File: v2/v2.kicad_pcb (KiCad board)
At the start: 4 copper layers, 45.5 x 52 mm, 73 parts, among them J1 Conn_01x02_Pin, J2 Conn_01x09_Pin, J3 Conn_01x20_Socket, J4 Conn_01x20_Socket, U1 ADS1299IPAGR, U11 TPS73225DBVR, U3 TPD4E1B06DCKR, U4 TPD4E1B06DCKR, U5 LM2664M6, U6 TPS61023DRLR, U7 TPS73233DBVT, U8 TPS72325DBVT, U9 TPD4E1B06DCKR

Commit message: v02 init placements
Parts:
- removed C25, C26, C31, C32, C33, C34, C35, C36, C37, C38, C39, C40, C41, C42, C43, C44: 1nF, Capacitor_SMD:C_0603_1608Metric_Pad1.08x0.95mm_HandSolder
- added CN1: W2A41C681KAT2A, CustomLib:CAP-ARRAY-SMD_6124-8P-L3.2-W1.6-BL, F.Cu at (165.8, 70.6)
- added CN2: W2A41C681KAT2A, CustomLib:CAP-ARRAY-SMD_6124-8P-L3.2-W1.6-BL, F.Cu at (165.8, 74.8)
- added CN3: W2A41C681KAT2A, CustomLib:CAP-ARRAY-SMD_6124-8P-L3.2-W1.6-BL, F.Cu at (165.8, 78.9)
- added CN4: W2A41C681KAT2A, CustomLib:CAP-ARRAY-SMD_6124-8P-L3.2-W1.6-BL, F.Cu at (165.8, 83.0)
- C1, C18, C19, C22, C3: footprint Capacitor_SMD:C_0805_2012Metric_Pad1.18x1.45mm_HandSolder -> Capacitor_SMD:C_0603_1608Metric_Pad1.08x0.95mm_HandSolder
- C10, C12, C14, C17, C27, C29, C4, C5, C9: footprint Capacitor_SMD:C_0402_1005Metric_Pad0.74x0.62mm_HandSolder -> Capacitor_SMD:C_0603_1608Metric_Pad1.08x0.95mm_HandSolder
- C13: footprint Capacitor_SMD:C_1210_3225Metric_Pad1.33x2.70mm_HandSolder -> Capacitor_SMD:C_1206_3216Metric_Pad1.33x1.80mm_HandSolder
- C20, C21, C24: footprint Capacitor_SMD:C_1210_3225Metric_Pad1.33x2.70mm_HandSolder -> Capacitor_SMD:C_0603_1608Metric_Pad1.08x0.95mm_HandSolder
- C23, C28, C30: footprint Capacitor_SMD:C_0201_0603Metric_Pad0.64x0.40mm_HandSolder -> Capacitor_SMD:C_0603_1608Metric_Pad1.08x0.95mm_HandSolder
- R1: footprint Resistor_SMD:R_0402_1005Metric_Pad0.72x0.64mm_HandSolder -> Resistor_SMD:R_0603_1608Metric_Pad0.98x0.95mm_HandSolder
- R10, R2, R3, R4, R5, R6, R7, R8, R9: footprint Resistor_SMD:R_0805_2012Metric_Pad1.20x1.40mm_HandSolder -> Resistor_SMD:R_0603_1608Metric_Pad0.98x0.95mm_HandSolder
- RN5, RN6, RN7, RN8: footprint CustomLib:CAT16A203J4LF -> CustomLib:RES-ARRAY-SMD_0603-8P-L3.2-W1.6-BL
- moved J1 67.6 mm to (127.7, 60.7)
- moved C30 45.2 mm to (173.3, 95.5)
- moved U11 41.4 mm to (174.2, 89.5)
- moved C29 41.2 mm to (173.3, 93.0)
- moved L1 34.1 mm to (204.5, 70.7)
- moved C28 33.8 mm to (181.0, 95.5)
- moved C21 33.1 mm to (198.4, 74.0)
- moved C20 32.0 mm to (198.4, 71.5)
- moved U6 30.6 mm to (202.3, 75.2)
- moved U7 30.0 mm to (181.9, 89.5)
- moved C27 29.8 mm to (181.0, 93.0)
- moved C19 29.3 mm to (198.4, 69.0)
- moved C1 25.3 mm to (173.3, 69.0)
- moved C14 24.4 mm to (173.3, 84.0)
- moved C10 23.4 mm to (173.3, 79.0)
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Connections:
- C1 pad 1: Net-(U1-BIASINV) -> Net-(U1-BIASIN)
- R1 pad 1: Net-(U1-BIASINV) -> Net-(U1-BIASIN)
- U1 pad 61: Net-(U1-BIASINV) -> unconnected-(U1-BIASINV-Pad61)
- U1 pad 62: /ADS1299/Bias -> Net-(U1-BIASIN)
- U1 pad 63: /ADS1299/Bias -> Net-(U1-BIASIN)
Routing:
- net -2V5: track 12.0 -> 0.18 mm, vias 1 -> 0

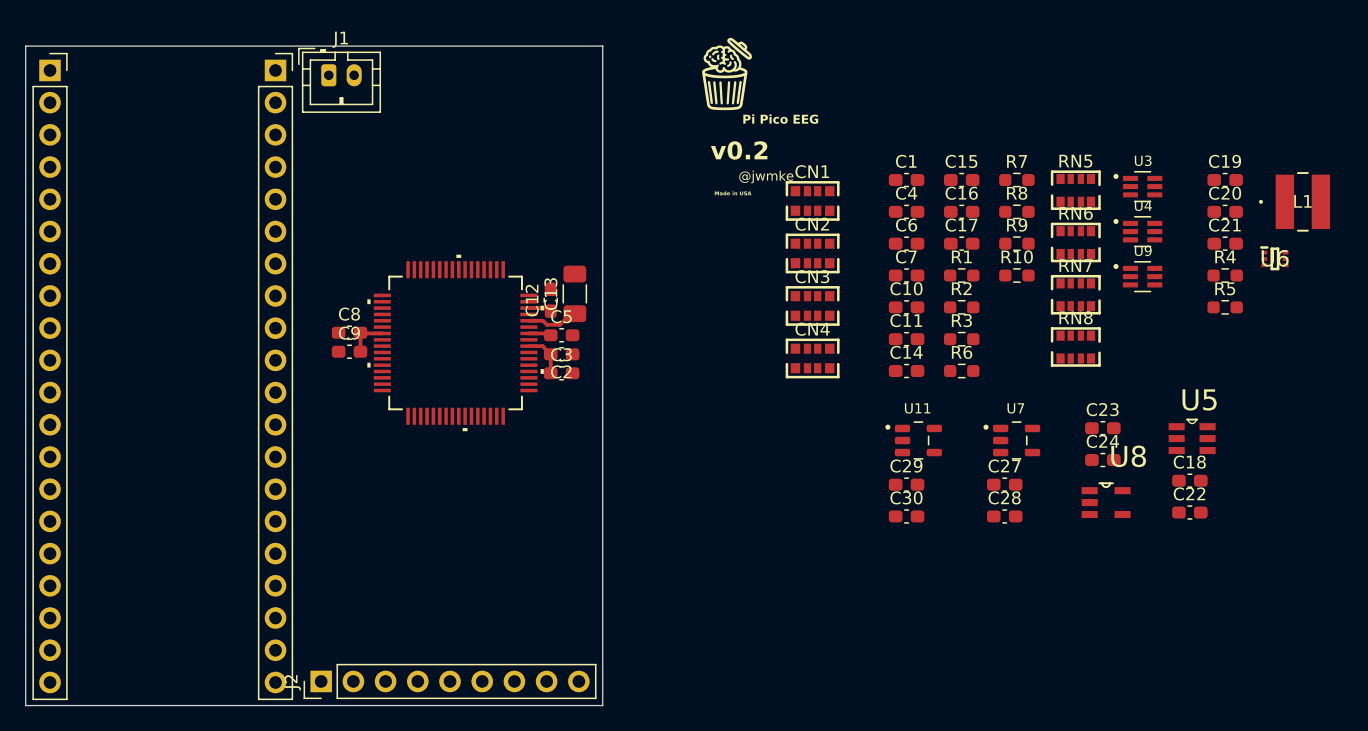
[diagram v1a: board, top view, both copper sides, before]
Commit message: v2 volt regs and grounding
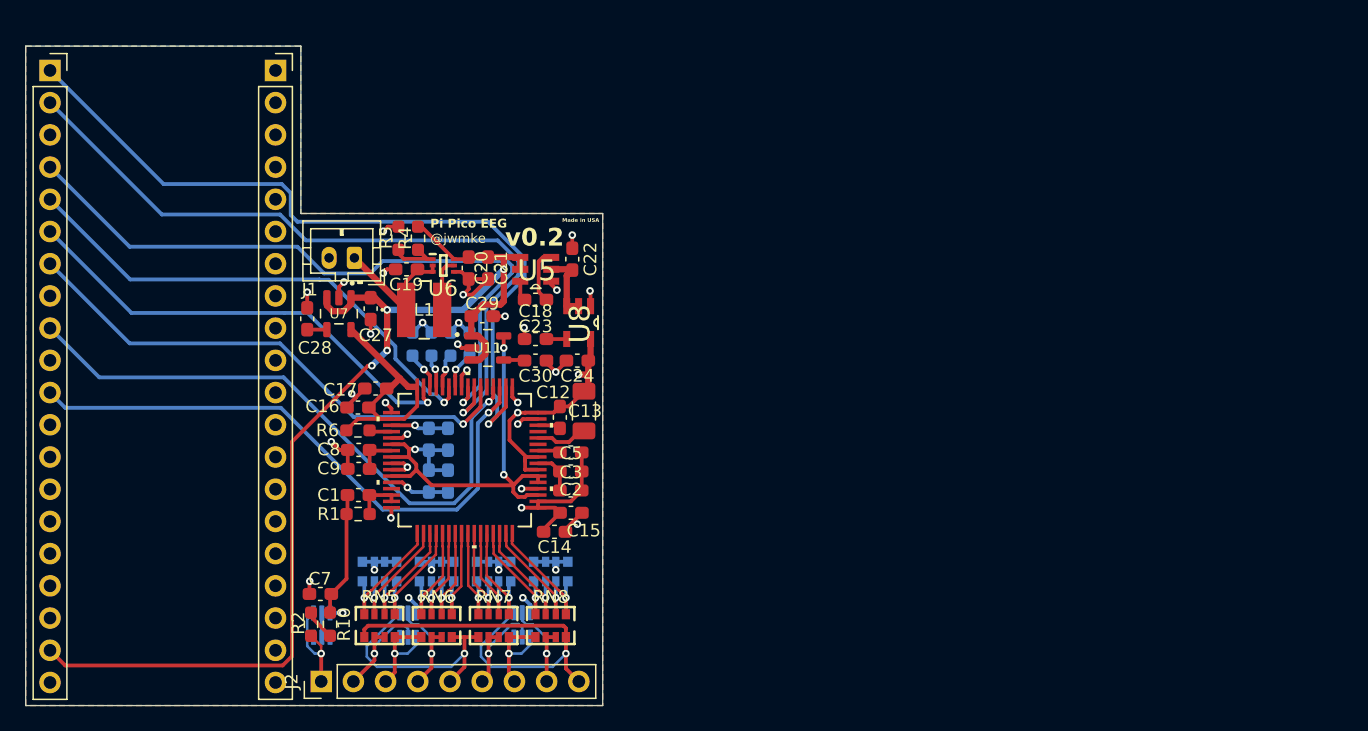
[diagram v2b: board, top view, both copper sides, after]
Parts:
- removed G***: LOGO, CustomLib:brain2
- C10, C11, C4, C6, CN1, CN2, CN3, CN4, R3, R7, R8, R9, U3, U4, U9: moved to B.Cu
- moved U9 70.3 mm to (127.2, 104.1), turned to -90 degrees
- moved L1 69.8 mm to (135.2, 79.2)
- moved U4 65.7 mm to (133.9, 104.1), turned to -90 degrees
- moved U6 65.6 mm to (136.7, 75.7)
- moved R5 65.4 mm to (133.2, 73.5), turned to 90 degrees
- moved C19 64.9 mm to (133.8, 76.0), turned to 180 degrees
- moved RN5 64.8 mm to (131.7, 104.1)
- moved R4 63.7 mm to (134.7, 73.5), turned to -90 degrees
- moved R10 60.7 mm to (127.8, 104.0), turned to -90 degrees
- moved U3 59.9 mm to (142.9, 104.0), turned to -90 degrees
- moved C20 59.8 mm to (138.7, 75.9), turned to 90 degrees
- moved RN6 58.8 mm to (136.2, 104.1)
- moved C21 58.2 mm to (140.3, 75.9), turned to 90 degrees
- moved C28 57.2 mm to (126.0, 79.9), turned to -90 degrees
- moved R2 57.1 mm to (126.3, 104.0), turned to -90 degrees
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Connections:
- CN1 pad 1: /ADS1299/IN2N -> /ADS1299/IN1P
- CN1 pad 2: /ADS1299/IN2P -> /ADS1299/IN1N
- CN1 pad 3: /ADS1299/IN1N -> /ADS1299/IN2P
- CN1 pad 4: /ADS1299/IN1P -> /ADS1299/IN2N
- CN2 pad 1: /ADS1299/IN4N -> /ADS1299/IN3P
- CN2 pad 2: /ADS1299/IN4P -> /ADS1299/IN3N
- CN2 pad 3: /ADS1299/IN3N -> /ADS1299/IN4P
- CN2 pad 4: /ADS1299/IN3P -> /ADS1299/IN4N
- CN3 pad 1: /ADS1299/IN6N -> /ADS1299/IN5P
- CN3 pad 2: /ADS1299/IN6P -> /ADS1299/IN5N
- CN3 pad 3: /ADS1299/IN5N -> /ADS1299/IN6P
- CN3 pad 4: /ADS1299/IN5P -> /ADS1299/IN6N
- CN4 pad 1: /ADS1299/IN8N -> /ADS1299/IN7P
- CN4 pad 2: /ADS1299/IN8P -> /ADS1299/IN7N
- CN4 pad 3: /ADS1299/IN7N -> /ADS1299/IN8P
- CN4 pad 4: /ADS1299/IN7P -> /ADS1299/IN8N
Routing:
- net +5V: track 0.00 -> 89.3 mm, vias 0 -> 4
- net GND: track 0.00 -> 63.6 mm, vias 0 -> 31
- net /ADS1299/MOSI: track 0.00 -> 62.6 mm, vias 0 -> 1
- net /ADS1299/CS: track 0.00 -> 58.4 mm, vias 0 -> 1
- net /ADS1299/SCLK: track 0.00 -> 54.2 mm, vias 0 -> 1
- net /ADS1299/RESET: track 0.00 -> 48.1 mm, vias 0 -> 1
- net /ADS1299/PDWN: track 0.00 -> 47.0 mm, vias 0 -> 1
- net -2V5: track 0.18 -> 44.3 mm, vias 0 -> 8
- net /ADS1299/START: track 0.00 -> 41.3 mm, vias 0 -> 1
- net /ADS1299/MISO: track 0.00 -> 39.8 mm, vias 0 -> 1
- net +2V5: track 0.00 -> 38.9 mm, vias 0 -> 3
- net /ADS1299/DRDY: track 0.00 -> 36.7 mm, vias 0 -> 1
- net /ADS1299/I1: track 0.00 -> 33.3 mm, vias 0 -> 1
- net +3V3: track 0.00 -> 20.5 mm
- net /ADS1299/I5: track 0.00 -> 19.1 mm, vias 0 -> 1
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- added copper zone on B.Cu, net (none)
- added copper zone on F.Cu, net (none)
- added copper zone on In2.Cu, net -2V5
- added copper zone on In1.Cu, net GND
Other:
- outline, holes or cut-outs redrawn
